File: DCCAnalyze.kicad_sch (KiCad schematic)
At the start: 31 parts, among them J1 RJ12, SW1 PWR_SEL, SW2 LEFT, SW3 UP, SW4 RIGHT, U1 6N137, U2 6N137

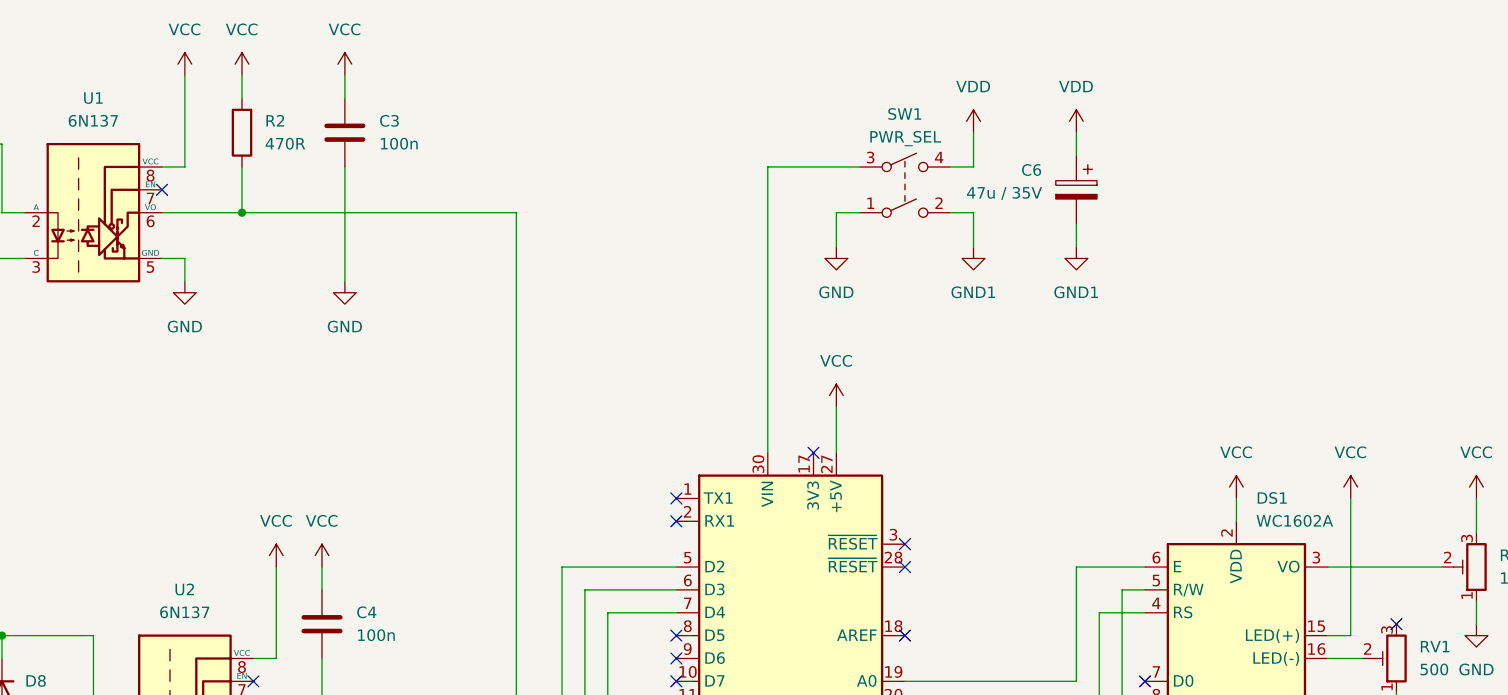
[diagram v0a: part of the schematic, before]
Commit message: Correct LCD value
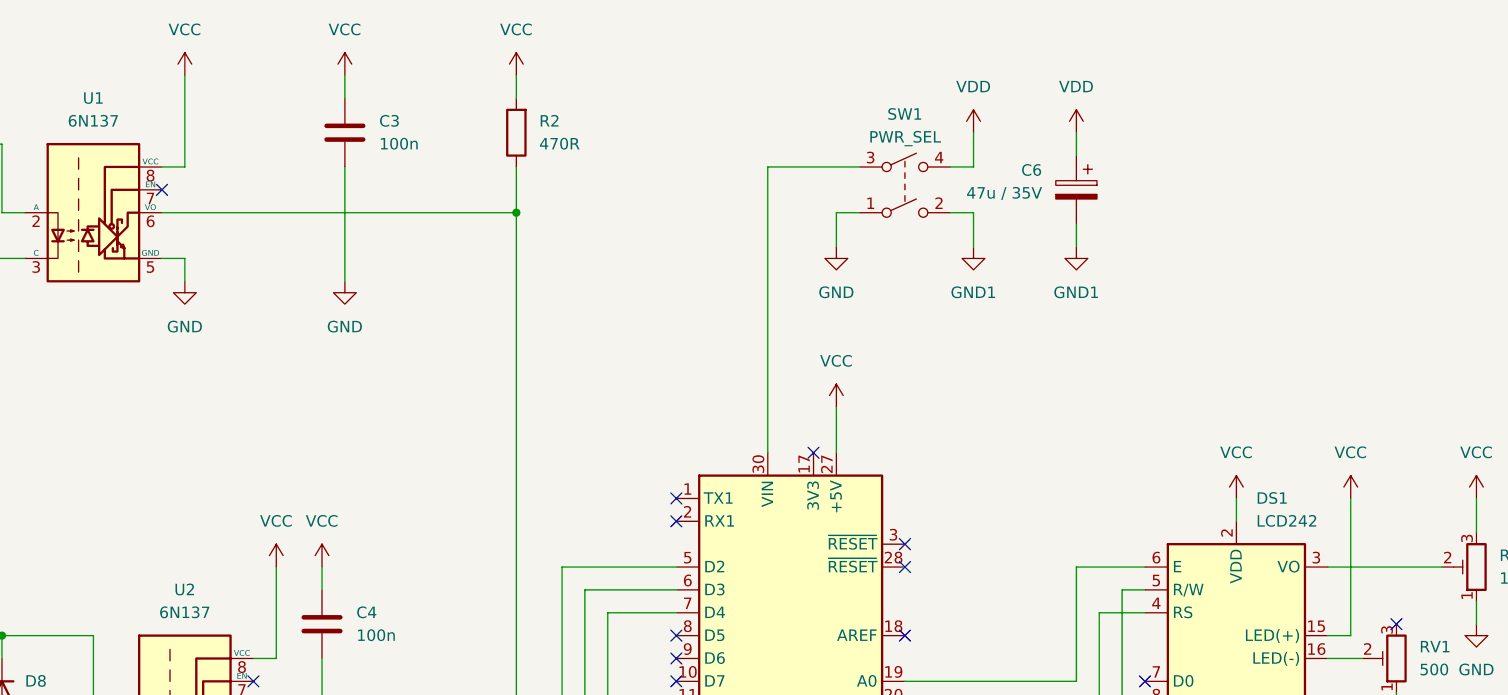
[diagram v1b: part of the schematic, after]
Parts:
- DS1: value WC1602A -> LCD242
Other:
- moved on the sheet: R2
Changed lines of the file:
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@@
 	)
 	(junction
+		(at 142.24 46.99)
+		(diameter 0)
+		(color 0 0 0 0)
+	)
+	(junction
 		(at 76.2 93.98)
 		(diameter 0)
@@
 	)
 	(junction
-		(at 111.76 46.99)
-		(diameter 0)
-		(color 0 0 0 0)
-	)
-	(junction
 		(at 43.18 49.53)
 		(diameter 0)
@@
 	(wire
 		(pts
-			(xy 111.76 46.99) (xy 142.24 46.99)
-		)
-		(stroke
-			(width 0)
-			(type default)
-		)
-	)
-	(wire
-		(pts
 			(xy 33.02 52.07) (xy 66.04 52.07)
 		)
@@
 	(wire
 		(pts
-			(xy 111.76 46.99) (xy 111.76 41.91)
-		)
-		(stroke
-			(width 0)
-			(type default)
-		)
-	)
-	(wire
-		(pts
 			(xy 85.09 106.68) (xy 97.79 106.68)
 		)
@@
 	(wire
 		(pts
-			(xy 111.76 31.75) (xy 111.76 34.29)
+			(xy 142.24 31.75) (xy 142.24 34.29)
 		)
 		(stroke
@@
 	(wire
 		(pts
+			(xy 142.24 41.91) (xy 142.24 46.99)
+		)
+		(stroke
+			(width 0)
+			(type default)
+		)
+	)
+	(wire
+		(pts
 			(xy 40.64 93.98) (xy 43.18 93.98)
 		)
@@
 	(wire
 		(pts
-			(xy 102.87 46.99) (xy 111.76 46.99)
+			(xy 102.87 46.99) (xy 142.24 46.99)
 		)
 		(stroke
@@
 			)
 		)
-		(property "Value" "WC1602A"
+		(property "Value" "LCD242"
 			(at 224.4441 81.28 0)
 			(effects
@@
 			)
 		)
-		(property "Description" "LCD 16x2 Alphanumeric , 8 bit parallel bus, 5V VDD"
+		(property "Description" "LCD 24x2 Alphanumeric , 8 bit parallel bus, 5V VDD"
 			(at 222.25 101.6 0)
 			(effects
@@
 	(symbol
 		(lib_id "power:VCC")
-		(at 111.76 31.75 0)
+		(at 142.24 31.75 0)
 		(unit 1)
 		(exclude_from_sim no)
@@
 		(fields_autoplaced yes)
 		(property "Reference" "#PWR015"
-			(at 111.76 35.56 0)
+			(at 142.24 35.56 0)
 			(effects
 				(font
@@
 		)
 		(property "Value" "VCC"
-			(at 111.76 26.67 0)
+			(at 142.24 26.67 0)
 			(effects
 				(font
@@
 		)
 		(property "Footprint" ""
-			(at 111.76 31.75 0)
+			(at 142.24 31.75 0)
 			(effects
 				(font
@@
 		)
 		(property "Datasheet" ""
-			(at 111.76 31.75 0)
+			(at 142.24 31.75 0)
 			(effects
 				(font
@@
 		)
 		(property "Description" "Power symbol creates a global label with name \"VCC\""
-			(at 111.76 31.75 0)
+			(at 142.24 31.75 0)
 			(effects
 				(font
@@
 	(symbol
 		(lib_id "Device:R")
-		(at 111.76 38.1 180)
+		(at 142.24 38.1 180)
 		(unit 1)
 		(exclude_from_sim no)
@@
 		(fields_autoplaced yes)
 		(property "Reference" "R2"
-			(at 114.3 36.8299 0)
+			(at 144.78 36.8299 0)
 			(effects
 				(font
@@
 		)
 		(property "Value" "470R"
-			(at 114.3 39.3699 0)
+			(at 144.78 39.3699 0)
 			(effects
 				(font
@@
 		)
 		(property "Footprint" "Resistor_SMD:R_1206_3216Metric_Pad1.30x1.75mm_HandSolder"
-			(at 113.538 38.1 90)
+			(at 144.018 38.1 90)
 			(effects
 				(font
@@
 		)
 		(property "Datasheet" "~"
-			(at 111.76 38.1 0)
+			(at 142.24 38.1 0)
 			(effects
 				(font
@@
 		)
 		(property "Description" "Resistor"
-			(at 111.76 38.1 0)
+			(at 142.24 38.1 0)
 			(effects
 				(font
